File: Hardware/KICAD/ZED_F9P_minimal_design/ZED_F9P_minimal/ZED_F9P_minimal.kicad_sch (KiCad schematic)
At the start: 21 parts, among them IC1 ZED-F9P-15B, J1 Conn_Coaxial_Small, U1 NCV8705ML33TCG

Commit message: fix backup
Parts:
- removed C3: 11pF, 11pF:CAPC1608X90, symbol Device:C
- removed C5: 2µF, 2_2uF:CAPC1608X90, symbol Device:C
- removed R2: 8.2ohm, 10_Ohm:RC0402N_YAG, symbol Device:R
- removed TP2, TP5: TestPoint, symbol Connector:TestPoint
- removed U1: NCV8705ML33TCG, LM5168F:DFNW8-3x3_ONS, symbol Voltage regulator:NCV8705ML33TCG
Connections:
- net GND: now also IC1.36 (V_BCKP), IC1.39 (USB_DM), IC1.40 (USB_DP), IC1.49 (RESET_N)
- net UART_RX: now also IC1.42 (TXD/SPI_SDO); no longer IC1.26 (RXD2)
- net UART_TX: now also IC1.43 (RXD/SPI_SDI); no longer IC1.27 (TXD2)
- net at C4.1, IC1.33 (VCC_1), IC1.34 (VCC_2)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: now also R1.2
- net I/O : now reaches IC1.44 (SDA/SPI_CS_N)
- net I/O_CLK_SELECT: now reaches IC1.45 (SCL/SPI_CLK)
- net O_TX_STATE: now reaches IC1.46 (TX_READY)
- net I_D_Sel: now reaches IC1.47 (D_SEL)
- net +3.3V renamed 12V ou 9V
- net 12V ou 9V: no longer IC1.36 (V_BCKP)
- net VCC_RF: no longer names the net of IC1.7 (VCC_RF)
- net VCC_RF: no longer R1.2
- no-connect marks 28 -> 29
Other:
- note added: "D_SEL=0 SPI_SD | D_SEL=1 UART from host"
- note added: "D_SEL=1 I2C_CLK / D_SEL=0 SPI_CLK (Input/Output)-"
- note added: "D_SEL=1 I2C_DATA / D_SEL=0 SPI Chip Select (Input/Output)-"
- note added: "Etat du registre TX (cf p.87)buffer full ou ready for data"
- note added: "RESET du F9P, supr ttes les infos et cold start,en dernier recours uniquement, état bas pdt 100ms pour trigger le reset"
- note added: "connecteur alim connecteur I et O UART"
- note added: "remplacer par nouveau regulo de tension ref sur mpmat/yassir"
- note removed: "D_SEL=1 I2C_DATA / D_SEL=0 SPI Chip Select (Input/Output)- D_SEL=1 I2C_CLK / D_SEL=0 SPI_CLK (Input/Output)-"
- note removed: "Etat du registre TX output- (cf p.87)buffer full ou ready for data"
- note removed: "RESET du F9P, supr ttes les infos et cold start,en dernier recours uniquement input- état bas pdt 100ms pour trigger le reset"
- note removed: "détermination de D_SEL (input)-"
- note removed: "filtre RC 1.76GHz"
- note removed: "input UART from chip output"
- note removed: "output- D_SEL=0 SPI_SD D_SEL=1 UART from host input-"
- moved on the sheet: C1, D1, R1, R4, R5, TP4

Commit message: Modification lisibilité
Modification lisibilité
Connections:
- net GND: no longer IC1.49 (RESET_N)
- new net I_RESET: IC1.49 (RESET_N)
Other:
- moved on the sheet: J1, TP1
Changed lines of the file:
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@@
 	)
 	(junction
-		(at 182.88 153.67)
-		(diameter 0)
-		(color 0 0 0 0)
-	)
-	(junction
 		(at 133.35 128.27)
 		(diameter 0)
@@
 	)
 	(junction
-		(at 134.62 153.67)
-		(diameter 0)
-		(color 0 0 0 0)
-	)
-	(junction
 		(at 191.77 148.59)
 		(diameter 0)
@@
 	)
 	(junction
-		(at 123.19 34.29)
+		(at 113.03 34.29)
 		(diameter 0)
 		(color 0 0 0 0)
@@
 	(wire
 		(pts
-			(xy 185.42 31.75) (xy 185.42 34.29)
-		)
-		(stroke
-			(width 0)
-			(type default)
-		)
-	)
-	(wire
-		(pts
 			(xy 133.35 115.57) (xy 133.35 113.03)
 		)
@@
 	(wire
 		(pts
-			(xy 185.42 34.29) (xy 182.88 34.29)
+			(xy 182.88 34.29) (xy 198.12 34.29)
 		)
 		(stroke
@@
 	(wire
 		(pts
-			(xy 182.88 153.67) (xy 134.62 153.67)
-		)
-		(stroke
-			(width 0)
-			(type default)
-		)
-	)
-	(wire
-		(pts
 			(xy 191.77 87.63) (xy 191.77 90.17)
 		)
@@
 	(wire
 		(pts
-			(xy 87.63 34.29) (xy 123.19 34.29)
-		)
-		(stroke
-			(width 0)
-			(type default)
-		)
-	)
-	(wire
-		(pts
 			(xy 191.77 115.57) (xy 191.77 118.11)
 		)
@@
 	(wire
 		(pts
-			(xy 123.19 34.29) (xy 134.62 34.29)
+			(xy 113.03 34.29) (xy 134.62 34.29)
 		)
 		(stroke
@@
 	(wire
 		(pts
-			(xy 57.15 22.86) (xy 60.96 22.86)
+			(xy 50.8 19.05) (xy 60.96 19.05)
 		)
 		(stroke
@@
 	(wire
 		(pts
-			(xy 60.96 27.94) (xy 60.96 29.21)
+			(xy 60.96 24.13) (xy 60.96 29.21)
 		)
 		(stroke
@@
 	(wire
 		(pts
-			(xy 77.47 34.29) (xy 87.63 34.29)
-		)
-		(stroke
-			(width 0)
-			(type default)
-		)
-	)
-	(wire
-		(pts
 			(xy 191.77 151.13) (xy 191.77 153.67)
 		)
@@
 	(wire
 		(pts
+			(xy 87.63 34.29) (xy 113.03 34.29)
+		)
+		(stroke
+			(width 0)
+			(type default)
+		)
+	)
+	(wire
+		(pts
 			(xy 133.35 120.65) (xy 134.62 120.65)
 		)
@@
 	(wire
 		(pts
-			(xy 123.19 153.67) (xy 123.19 151.13)
-		)
-		(stroke
-			(width 0)
-			(type default)
-		)
-	)
-	(wire
-		(pts
 			(xy 191.77 143.51) (xy 191.77 146.05)
 		)
@@
 	(wire
 		(pts
+			(xy 77.47 34.29) (xy 87.63 34.29)
+		)
+		(stroke
+			(width 0)
+			(type default)
+		)
+	)
+	(wire
+		(pts
 			(xy 113.03 124.46) (xy 113.03 125.73)
 		)
@@
 	(wire
 		(pts
-			(xy 31.75 151.13) (xy 123.19 151.13)
+			(xy 31.75 153.67) (xy 134.62 153.67)
 		)
 		(stroke
@@
 	(wire
 		(pts
-			(xy 57.15 22.86) (xy 57.15 24.13)
-		)
-		(stroke
-			(width 0)
-			(type default)
-		)
-	)
-	(wire
-		(pts
-			(xy 123.19 153.67) (xy 134.62 153.67)
+			(xy 50.8 19.05) (xy 50.8 24.13)
 		)
 		(stroke
@@
 	(wire
 		(pts
-			(xy 185.42 31.75) (xy 194.31 31.75)
-		)
-		(stroke
-			(width 0)
-			(type default)
-		)
-	)
-	(wire
-		(pts
 			(xy 191.77 140.97) (xy 182.88 140.97)
 		)
@@
 	(text "-output Sortie timer\n(si on veut ssynchro des choses dessus)"
 		(exclude_from_sim no)
-		(at 192.278 35.306 0)
+		(at 196.088 37.846 0)
 		(effects
 			(font
@@
 	(text "connecteur alim\nconnecteur I et O UART\n"
 		(exclude_from_sim no)
-		(at 23.622 156.718 0)
+		(at 23.876 160.02 0)
 		(effects
 			(font
@@
 	)
 	(label "I_RESET"
-		(at 33.02 151.13 0)
+		(at 33.02 153.67 0)
 		(fields_autoplaced yes)
 		(effects
@@
 	)
 	(label "RF_IN"
-		(at 115.57 34.29 0)
+		(at 105.41 34.29 0)
 		(fields_autoplaced yes)
 		(effects
@@
 	(global_label "I_RESET"
 		(shape input)
-		(at 31.75 151.13 180)
+		(at 31.75 153.67 180)
 		(fields_autoplaced yes)
 		(effects
@@
 		)
 		(property "Intersheetrefs" "${INTERSHEET_REFS}"
-			(at 21.4473 151.13 0)
+			(at 21.4473 153.67 0)
 			(effects
 				(font
@@
 	(global_label "TIMER"
 		(shape output)
-		(at 194.31 31.75 0)
+		(at 198.12 34.29 0)
 		(fields_autoplaced yes)
 		(effects
@@
 		)
 		(property "Intersheetrefs" "${INTERSHEET_REFS}"
-			(at 202.738 31.75 0)
+			(at 206.548 34.29 0)
 			(effects
 				(font
@@
 	(symbol
 		(lib_id "Connector:TestPoint")
-		(at 123.19 34.29 0)
+		(at 113.03 34.29 0)
 		(unit 1)
 		(exclude_from_sim no)
@@
 		(fields_autoplaced yes)
 		(property "Reference" "TP1"
-			(at 125.73 29.7179 0)
+			(at 115.57 29.7179 0)
 			(effects
 				(font
@@
 		)
 		(property "Value" "TestPoint"
-			(at 125.73 32.2579 0)
+			(at 115.57 32.2579 0)
 			(effects
 				(font
@@
 		)
 		(property "Footprint" ""
-			(at 128.27 34.29 0)
+			(at 118.11 34.29 0)
 			(effects
 				(font
@@
 		)
 		(property "Datasheet" "~"
-			(at 128.27 34.29 0)
+			(at 118.11 34.29 0)
 			(effects
 				(font
@@
 		)
 		(property "Description" "test point"
-			(at 123.19 34.29 0)
+			(at 113.03 34.29 0)
 			(effects
 				(font
@@
 	(symbol
 		(lib_id "Connector:Conn_Coaxial_Small")
-		(at 60.96 25.4 90)
+		(at 60.96 21.59 90)
 		(unit 1)
 		(exclude_from_sim no)
@@
 		(fields_autoplaced yes)
 		(property "Reference" "J1"
-			(at 63.5 24.6494 90)
+			(at 63.5 20.8394 90)
 			(effects
 				(font
@@
 		)
 		(property "Value" "Conn_Coaxial_Small"
-			(at 63.5 27.1894 90)
+			(at 63.5 23.3794 90)
 			(effects
 				(font
@@
 		)
 		(property "Footprint" "SMA:RFSOLUTIONS_CON-SMA-EDGE-S"
-			(at 60.96 25.4 0)
+			(at 60.96 21.59 0)
 			(effects
 				(font
@@
 		)
 		(property "Datasheet" "~"
-			(at 60.96 25.4 0)
+			(at 60.96 21.59 0)
 			(effects
 				(font
@@
 		)
 		(property "Description" "small coaxial connector (BNC, SMA, SMB, SMC, Cinch/RCA, LEMO, ...)"
-			(at 60.96 25.4 0)
+			(at 60.96 21.59 0)
 			(effects
 				(font
@@
 		(on_board yes)
 		(dnp no)
-		(fields_autoplaced yes)
 		(property "Reference" "TP3"
-			(at 57.658 24.13 90)
+			(at 54.864 29.21 90)
 			(effects
 				(font
@@
 		)
 		(property "Value" "TestPoint"
-			(at 57.658 26.67 90)
+			(at 57.15 27.432 90)
 			(effects
 				(font
@@
 	(symbol
 		(lib_id "power:GND")
-		(at 57.15 24.13 0)
+		(at 50.8 24.13 0)
 		(unit 1)
 		(exclude_from_sim no)
@@
 		(dnp no)
 		(property "Reference" "#PWR06"
-			(at 57.15 30.48 0)
+			(at 50.8 30.48 0)
 			(effects
 				(font
@@
 		)
 		(property "Value" "GND"
-			(at 54.864 24.384 0)
+			(at 48.514 24.384 0)
 			(effects
 				(font
@@
 		)
 		(property "Footprint" ""
-			(at 57.15 24.13 0)
+			(at 50.8 24.13 0)
 			(effects
 				(font
@@
 		)
 		(property "Datasheet" ""
-			(at 57.15 24.13 0)
+			(at 50.8 24.13 0)
 			(effects
 				(font
@@
 		)
 		(property "Description" "Power symbol creates a global label with name \"GND\" , ground"
-			(at 57.15 24.13 0)
+			(at 50.8 24.13 0)
 			(effects
 				(font

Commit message: finalised first iteration of schematic
schematic 1.0,, gonna start pcb rooting
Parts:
- removed C1: 10µF, 1uF:YAG_CC0603_YAG, symbol Device:C
- removed IC1: ZED-F9P-15B, RF_GPS:ublox_ZED, symbol ZED-F9P-15B:ZED-F9P-15B
- removed R4: 120, 120ohm:RC0805N_YAG, symbol Device:R
- added C5, C6: 100nF, Capacitor_SMD:C_0805_2012Metric, symbol Device:C
- added J2: DF11-18DS-2DSA06, Connector:CON18_2X9_U_DF11_HIR, symbol CON2x09:DF11-18DS-2DSA06
- added JP1, JP2, JP3, JP4: Jumper_2_Open, Connector:CON_1x02, symbol Jumper:Jumper_2_Open
- added R2, R6: 10k, res_SMD_10kohm:YAG_R0805_YAG, symbol Device:R
- added R3: 3.9k, res_SMD_4.3kohm:RC0805N_YAG, symbol Device:R
- added R7: 5.6k, res_SMD_5.6kohm:RC0805N_YAG, symbol Device:R
- added TP2, TP5: TestPoint, TestPoint:CONN1_5011_KEY, symbol Connector:TestPoint
- added U1: OPA2365AID, 00_OPA2365:D8, symbol OPA2365:OPA2365AID
- added U2: LM1086IT-ADJ/NOPB, LM1086:NDE0003B, symbol LM1086:LM1086IT-ADJ_NOPB
- added U3: ZED-F9P, RF_GPS:ublox_ZED, symbol RF_GPS:ZED-F9P
- C2: value 100nf_16V -> 100nf; footprint 0_1uF:YAG_CC0603_YAG -> Capacitor_SMD:C_0805_2012Metric
- C4: footprint 1uF:YAG_CC0603_YAG -> Capacitor_SMD:C_0805_2012Metric
- D1: value EASR3216RA0 -> LED_rouge; footprint (none) -> LED_SMD:LED_0805_2012Metric
- D2: value D_Zener -> 3.6; footprint (none) -> Diode_SMD:Zener_3.6V
- D3: value D_TVS -> 3.7; footprint (none) -> Diode_SMD:D_SOD962_TVS_3.7V
- L1: footprint 0_01uH:STA_RMCF1206_STP -> Inductor_SMD:L_0805_2012Metric
- R1: footprint 10_Ohm:RC0402N_YAG -> res_SMD_330ohm:RC0805N_YAG
- R5: footprint 330_ohm:RC0603N_YAG -> res_SMD_330ohm:RC0805N_YAG
- TP1, TP3, TP4: footprint (none) -> TestPoint:CONN1_5011_KEY
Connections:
- net GND: now also C5.2, C6.2, J2.9, R3.2, R7.2, U1.4 (V-), U2.1 (GND), U3.1 (GND), U3.12 (GND), U3.14 (GND), U3.3 (GND), U3.32 (GND), U3.36 (V_BCKP), U3.37 (GND), U3.38 (V_USB), U3.39 (USB_DM), U3.40 (USB_DP), U3.41 (GND), U3.48 (GND), U3.55 (GND), U3.7 (VCC_RF)
- net I_D_Sel: now also J2.3, U3.47 (D_SEL)
- net I_RESET: now also J2.2, U3.49 (~{RESET})
- net I/O : now also J2.6, U3.44 (SDA/~{SPI_CS})
- net I/O_CLK_SELECT: now also J2.5, U3.45 (SCL/SPI_CLK)
- net O_TX_STATE: now also J2.4, U3.46 (TX_READY)
- net RF_IN: now also U3.2 (RF_IN)
- net TIMER: now also J2.1, U3.53 (TIMEPULSE)
- net UART_RX: now also J2.8, U3.43 (RXD/SPI_MOSI)
- net UART_TX: now also J2.7, U3.42 (TXD/SPI_MISO)
- net 3v3_puce: now reaches C4.1, TP4.1
- net 3v3_puce: now also U1.1 (VOUTA), U1.2 (INA-), U3.33 (VCC), U3.34 (VCC); no longer R1.2
- net at R5.1: now also U3.20 (RTK_STAT)
- new net: C5.1, C6.1, R2.1, R6.1, U2.2 (OUTPUT)
- new net 12V: J2.18, U1.8 (V+), U2.3 (INPUT)
- new net 3V3-IN: JP1.1 (A), R2.2, R3.1, TP2.1
- new net 3V3-jumper: J2.17, JP2.1 (A)
- new net 5V-IN: JP3.1 (A), R6.2, R7.1, TP5.1
- new net 5V-jumper: J2.16, JP4.1 (A)
- new net 5v_antenne: R1.2, U1.6 (INB-), U1.7 (VOUTB)
- new net jumper_3V_out: JP1.2 (B), JP2.2 (B), U1.3 (INA+)
- new net jumper_5V_out: JP3.2 (B), JP4.2 (B), U1.5 (INB+)
- no-connect marks 29 -> 12
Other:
- note removed: "(input/output)- USB DATA"
- note removed: "Les PORTs UART DOIVENT etre déplacer sur les PIN 42 et 43 Pour utiliser UART 1 et non 2 UART 2 a des fonctionaliser en moins :)"
- note removed: "connecteur alim connecteur I et O UART"
- note removed: "contacter ublox pour model PSPICE de la puce"
- note removed: "remplacer par nouveau regulo de tension ref sur mpmat/yassir"
- moved on the sheet: C2, C4, D1, D2, D3, J1, L1, R1, R5, TP1, TP3, TP4

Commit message: changed diode footprint
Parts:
- D2: footprint Diode_SMD:Zener_3.6V -> Diode_SMD:D_SOD-323
- D3: footprint Diode_SMD:D_SOD962_TVS_3.7V -> Diode_SMD:D_0805_2012Metric
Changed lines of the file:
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@@
 			)
 		)
-		(property "Footprint" "Diode_SMD:D_SOD962_TVS_3.7V"
+		(property "Footprint" "Diode_SMD:D_0805_2012Metric"
 			(at 105.41 52.07 0)
 			(effects
@@
 			)
 		)
-		(property "Footprint" "Diode_SMD:Zener_3.6V"
+		(property "Footprint" "Diode_SMD:D_SOD-323"
 			(at 95.25 50.8 0)
 			(effects

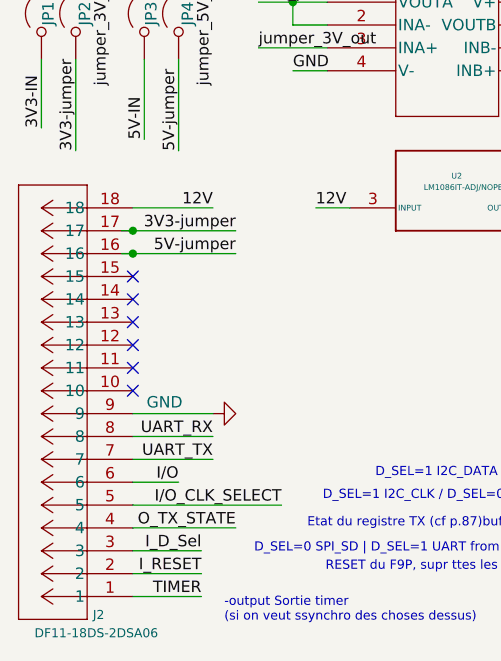
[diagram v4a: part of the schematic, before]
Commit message: Z9P PCB
arranged placement, rooting still to do
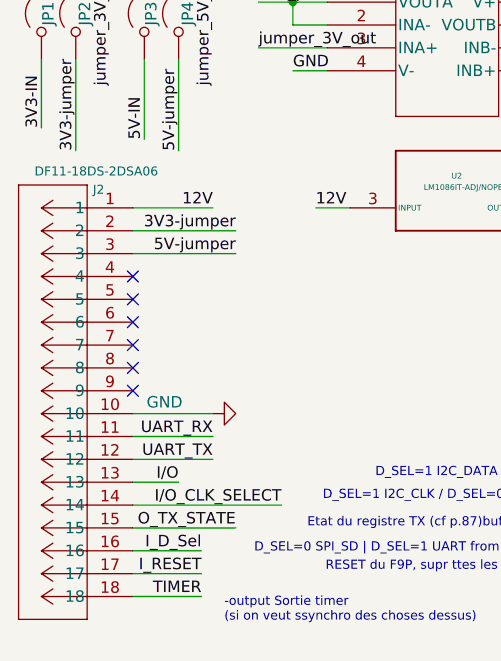
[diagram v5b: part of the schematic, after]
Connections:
- net 12V: now also J2.1; no longer J2.18
- net 3V3-jumper: now also J2.2; no longer J2.17
- net 5V-jumper: now also J2.3; no longer J2.16
- net GND: now also J2.10; no longer J2.9
- net I_D_Sel: now also J2.16; no longer J2.3
- net I_RESET: now also J2.17; no longer J2.2
- net I/O : now also J2.13; no longer J2.6
- net I/O_CLK_SELECT: now also J2.14; no longer J2.5
- net O_TX_STATE: now also J2.15; no longer J2.4
- net TIMER: now also J2.18; no longer J2.1
- net UART_RX: now also J2.11; no longer J2.8
- net UART_TX: now also J2.12; no longer J2.7
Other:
- moved on the sheet: J2
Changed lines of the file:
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@@
-	)
-	(junction
-		(at 44.45 109.22)
-		(diameter 0)
-		(color 0 0 0 0)
 	)
 	(junction
@@
 	)
 	(junction
-		(at 44.45 111.76)
-		(diameter 0)
-		(color 0 0 0 0)
-	)
-	(junction
 		(at 107.95 110.49)
 		(diameter 0)
@@
 	(wire
 		(pts
+			(xy 44.45 109.22) (xy 55.88 109.22)
+		)
+		(stroke
+			(width 0)
+			(type default)
+		)
+	)
+	(wire
+		(pts
 			(xy 154.94 35.56) (xy 153.67 35.56)
 		)
@@
 	(wire
 		(pts
-			(xy 44.45 109.22) (xy 55.88 109.22)
-		)
-		(stroke
-			(width 0)
-			(type default)
-		)
-	)
-	(wire
-		(pts
-			(xy 43.18 111.76) (xy 44.45 111.76)
-		)
-		(stroke
-			(width 0)
-			(type default)
-		)
-	)
-	(wire
-		(pts
 			(xy 115.57 100.33) (xy 115.57 104.14)
 		)
@@
 	(wire
 		(pts
+			(xy 105.41 40.64) (xy 105.41 48.26)
+		)
+		(stroke
+			(width 0)
+			(type default)
+		)
+	)
+	(wire
+		(pts
+			(xy 95.25 55.88) (xy 105.41 55.88)
+		)
+		(stroke
+			(width 0)
+			(type default)
+		)
+	)
+	(wire
+		(pts
+			(xy 154.94 35.56) (xy 154.94 41.91)
+		)
+		(stroke
+			(width 0)
+			(type default)
+		)
+	)
+	(wire
+		(pts
+			(xy 34.29 97.79) (xy 34.29 90.17)
+		)
+		(stroke
+			(width 0)
+			(type default)
+		)
+	)
+	(wire
+		(pts
+			(xy 44.45 132.08) (xy 53.34 132.08)
+		)
+		(stroke
+			(width 0)
+			(type default)
+		)
+	)
+	(wire
+		(pts
+			(xy 167.64 52.07) (xy 167.64 49.53)
+		)
+		(stroke
+			(width 0)
+			(type default)
+		)
+	)
+	(wire
+		(pts
+			(xy 62.23 83.82) (xy 62.23 86.36)
+		)
+		(stroke
+			(width 0)
+			(type default)
+		)
+	)
+	(wire
+		(pts
+			(xy 130.81 87.63) (xy 132.08 87.63)
+		)
+		(stroke
+			(width 0)
+			(type default)
+		)
+	)
+	(wire
+		(pts
+			(xy 111.76 82.55) (xy 111.76 90.17)
+		)
+		(stroke
+			(width 0)
+			(type default)
+		)
+	)
+	(wire
+		(pts
+			(xy 95.25 55.88) (xy 95.25 54.61)
+		)
+		(stroke
+			(width 0)
+			(type default)
+		)
+	)
+	(wire
+		(pts
+			(xy 38.1 100.33) (xy 38.1 90.17)
+		)
+		(stroke
+			(width 0)
+			(type default)
+		)
+	)
+	(wire
+		(pts
+			(xy 95.25 40.64) (xy 105.41 40.64)
+		)
+		(stroke
+			(width 0)
+			(type default)
+		)
+	)
+	(wire
+		(pts
+			(xy 44.45 149.86) (xy 52.07 149.86)
+		)
+		(stroke
+			(width 0)
+			(type default)
+		)
+	)
+	(wire
+		(pts
+			(xy 167.64 74.93) (xy 170.18 74.93)
+		)
+		(stroke
+			(width 0)
+			(type default)
+		)
+	)
+	(wire
+		(pts
 			(xy 44.45 111.76) (xy 55.88 111.76)
 		)
@@
 	(wire
 		(pts
-			(xy 105.41 40.64) (xy 105.41 48.26)
-		)
-		(stroke
-			(width 0)
-			(type default)
-		)
-	)
-	(wire
-		(pts
-			(xy 95.25 55.88) (xy 105.41 55.88)
-		)
-		(stroke
-			(width 0)
-			(type default)
-		)
-	)
-	(wire
-		(pts
-			(xy 154.94 35.56) (xy 154.94 41.91)
-		)
-		(stroke
-			(width 0)
-			(type default)
-		)
-	)
-	(wire
-		(pts
-			(xy 34.29 97.79) (xy 34.29 90.17)
-		)
-		(stroke
-			(width 0)
-			(type default)
-		)
-	)
-	(wire
-		(pts
-			(xy 44.45 132.08) (xy 53.34 132.08)
-		)
-		(stroke
-			(width 0)
-			(type default)
-		)
-	)
-	(wire
-		(pts
-			(xy 167.64 52.07) (xy 167.64 49.53)
-		)
-		(stroke
-			(width 0)
-			(type default)
-		)
-	)
-	(wire
-		(pts
-			(xy 62.23 83.82) (xy 62.23 86.36)
-		)
-		(stroke
-			(width 0)
-			(type default)
-		)
-	)
-	(wire
-		(pts
-			(xy 130.81 87.63) (xy 132.08 87.63)
-		)
-		(stroke
-			(width 0)
-			(type default)
-		)
-	)
-	(wire
-		(pts
-			(xy 111.76 82.55) (xy 111.76 90.17)
-		)
-		(stroke
-			(width 0)
-			(type default)
-		)
-	)
-	(wire
-		(pts
-			(xy 95.25 55.88) (xy 95.25 54.61)
-		)
-		(stroke
-			(width 0)
-			(type default)
-		)
-	)
-	(wire
-		(pts
-			(xy 38.1 100.33) (xy 38.1 90.17)
-		)
-		(stroke
-			(width 0)
-			(type default)
-		)
-	)
-	(wire
-		(pts
-			(xy 95.25 40.64) (xy 105.41 40.64)
-		)
-		(stroke
-			(width 0)
-			(type default)
-		)
-	)
-	(wire
-		(pts
-			(xy 44.45 149.86) (xy 52.07 149.86)
-		)
-		(stroke
-			(width 0)
-			(type default)
-		)
-	)
-	(wire
-		(pts
-			(xy 167.64 74.93) (xy 170.18 74.93)
-		)
-		(stroke
-			(width 0)
-			(type default)
-		)
-	)
-	(wire
-		(pts
 			(xy 44.45 106.68) (xy 53.34 106.68)
 		)
@@
 		(pts
 			(xy 95.25 110.49) (xy 101.6 110.49)
-		)
-		(stroke
-			(width 0)
-			(type default)
-		)
-	)
-	(wire
-		(pts
-			(xy 43.18 109.22) (xy 44.45 109.22)
 		)
 		(stroke
@@
 	(symbol
 		(lib_id "CON2x09:DF11-18DS-2DSA06")
-		(at 44.45 149.86 180)
+		(at 44.45 106.68 0)
+		(mirror y)
 		(unit 1)
 		(exclude_from_sim no)
@@
 		(dnp no)
 		(property "Reference" "J2"
-			(at 40.64 151.892 0)
+			(at 40.64 104.648 0)
 			(effects
 				(font
@@
 		)
 		(property "Value" "DF11-18DS-2DSA06"
-			(at 40.386 153.924 0)
+			(at 40.386 102.616 0)
 			(effects
 				(font
@@
 		)
 		(property "Footprint" "Connector:CON18_2X9_U_DF11_HIR"
-			(at 44.45 149.86 0)
+			(at 44.45 106.68 0)
 			(effects
 				(font
@@
 		)
 		(property "Datasheet" "DF11-18DS-2DSA06"
-			(at 44.45 149.86 0)
+			(at 44.45 106.68 0)
 			(effects
 				(font
@@
 		)
 		(property "Description" ""
-			(at 44.45 149.86 0)
+			(at 44.45 106.68 0)
 			(effects
 				(font
@@
 		)
 		(property "Height" ""
-			(at 44.45 149.86 0)
+			(at 44.45 106.68 0)
 			(effects
 				(font
@@
 		)
 		(property "Manufacturer_Name" ""
-			(at 44.45 149.86 0)
+			(at 44.45 106.68 0)
 			(effects
 				(font
@@
 		)
 		(property "Manufacturer_Part_Number" ""
-			(at 44.45 149.86 0)
+			(at 44.45 106.68 0)
 			(effects
 				(font
@@
 		)
 		(property "Mouser Part Number" ""
-			(at 44.45 149.86 0)
+			(at 44.45 106.68 0)
 			(effects
 				(font
@@
 		)
 		(property "Mouser Price/Stock" ""
-			(at 44.45 149.86 0)
-			(effects
-				(font
+			(at 44.45 106.68 0)
+			(effects
+				(font
